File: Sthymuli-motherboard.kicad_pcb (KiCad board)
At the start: 2 copper layers, 277 parts, among them J1 USB_C_Receptacle_USB2.0_16P, J2 Conn_01x09, J3 Conn_01x03, Q1 Q_NMOS_Depletion_GSD, Q10 NX7002AK, Q11 NX7002AK, Q12 NX7002AK, Q13 NX7002AK, Q14 NX7002AK, Q15 NX7002AK, Q2 Q_NMOS_Depletion_GSD, Q3 Q_NMOS_Depletion_GSD, Q4 Q_NMOS_Depletion_GSD, Q5 Q_NMOS_Depletion_GSD, Q6 Q_NMOS_Depletion_GSD, Q7 PMOS, Q8 NX7002AK, Q9 NX7002AK, SW1 SW_Push, SW10 SW_Push, SW2 SW_Push, SW3 SW_Push, SW4 SW_Push, SW5 SW_Push, SW6 SW_Push, SW7 SW_Push, SW8 SW_Push, SW9 SW_Push, U1 ESP32-S3-WROOM-1, U10 74HC4051, U11 MCP6L01x-xOT, U12 74HC4051, U13 LSM6DS3, U14 LSM6DS3, U15 ITR9909, U16 ITR9909, U17 ITR9909, U18 ITR9909, U19 ITR9909, U2 AP2112K-3.3, U20 ITR9909, U21 ITR9909, U22 ITR9909, U3 BQ76905RGRR, U4 AP62300WU, U5 BQ25713, U6 AP62300WU, U7 MCP23017_SO, U8 AP22913CN4, U9 IRM-H6xxT

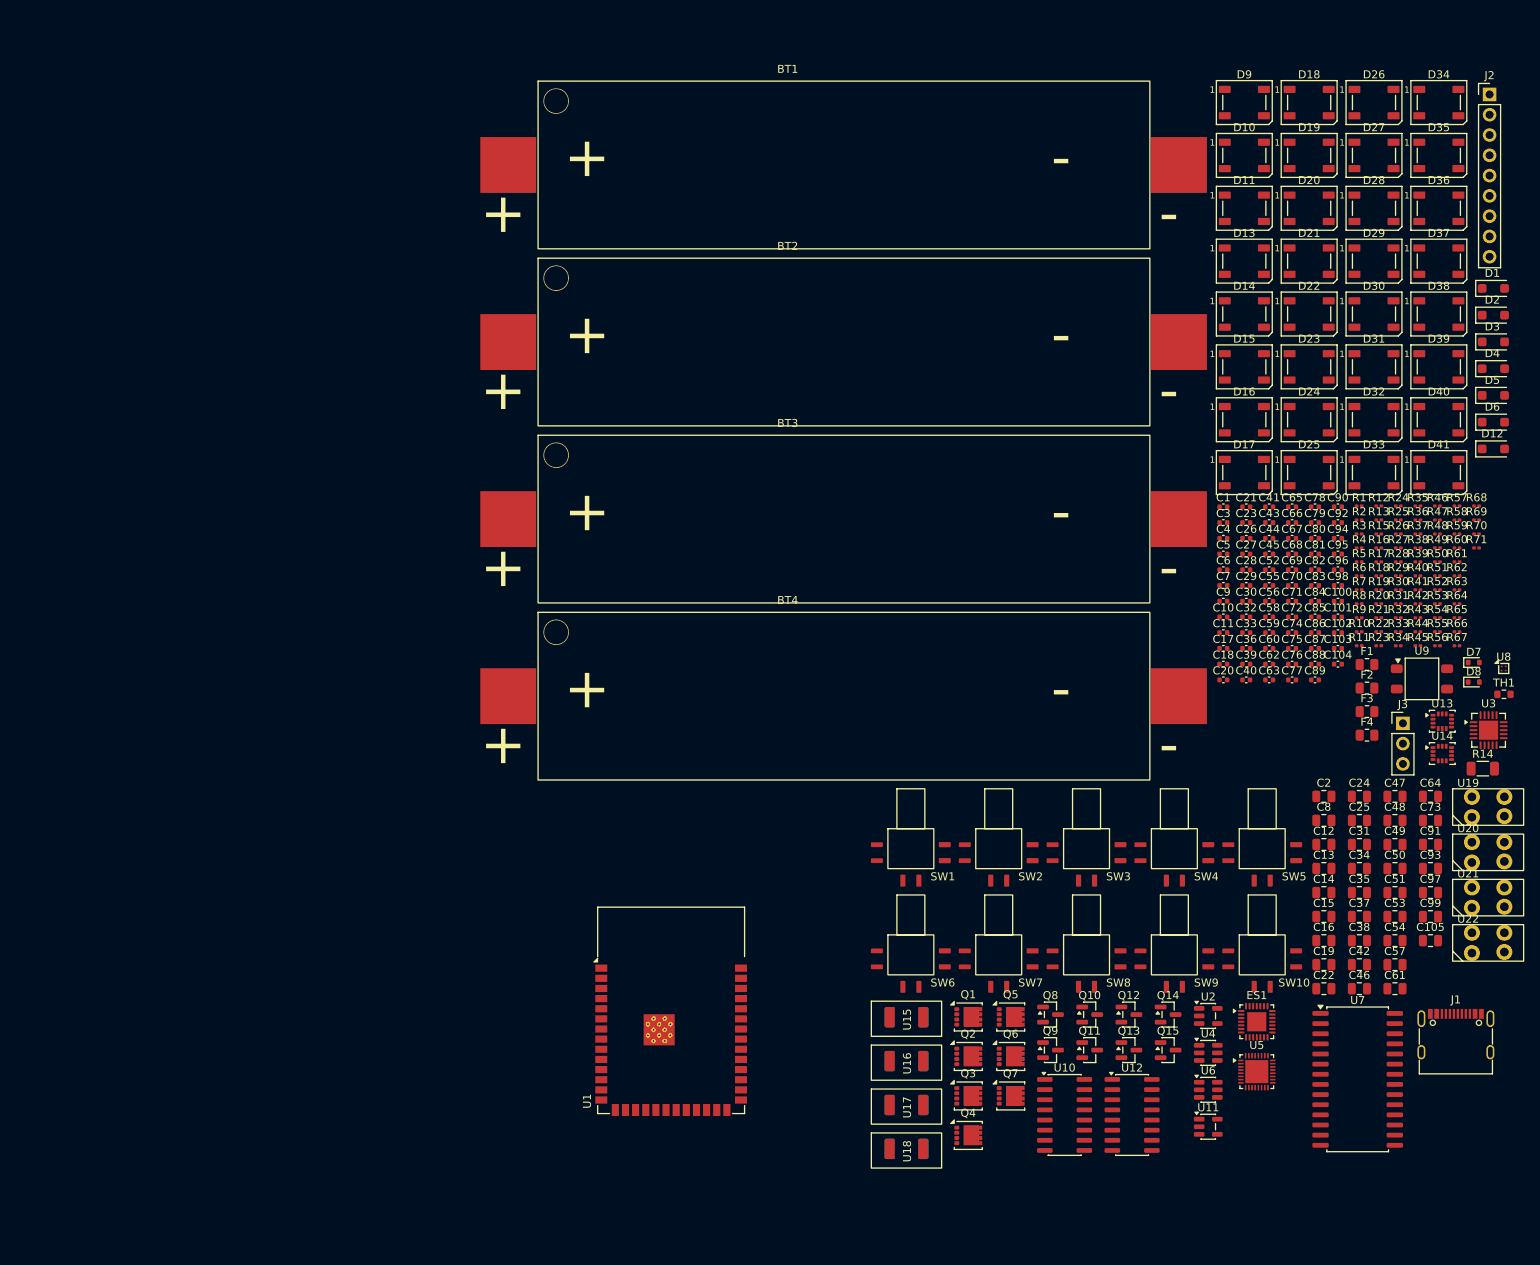
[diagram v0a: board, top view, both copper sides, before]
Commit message: started layout of component
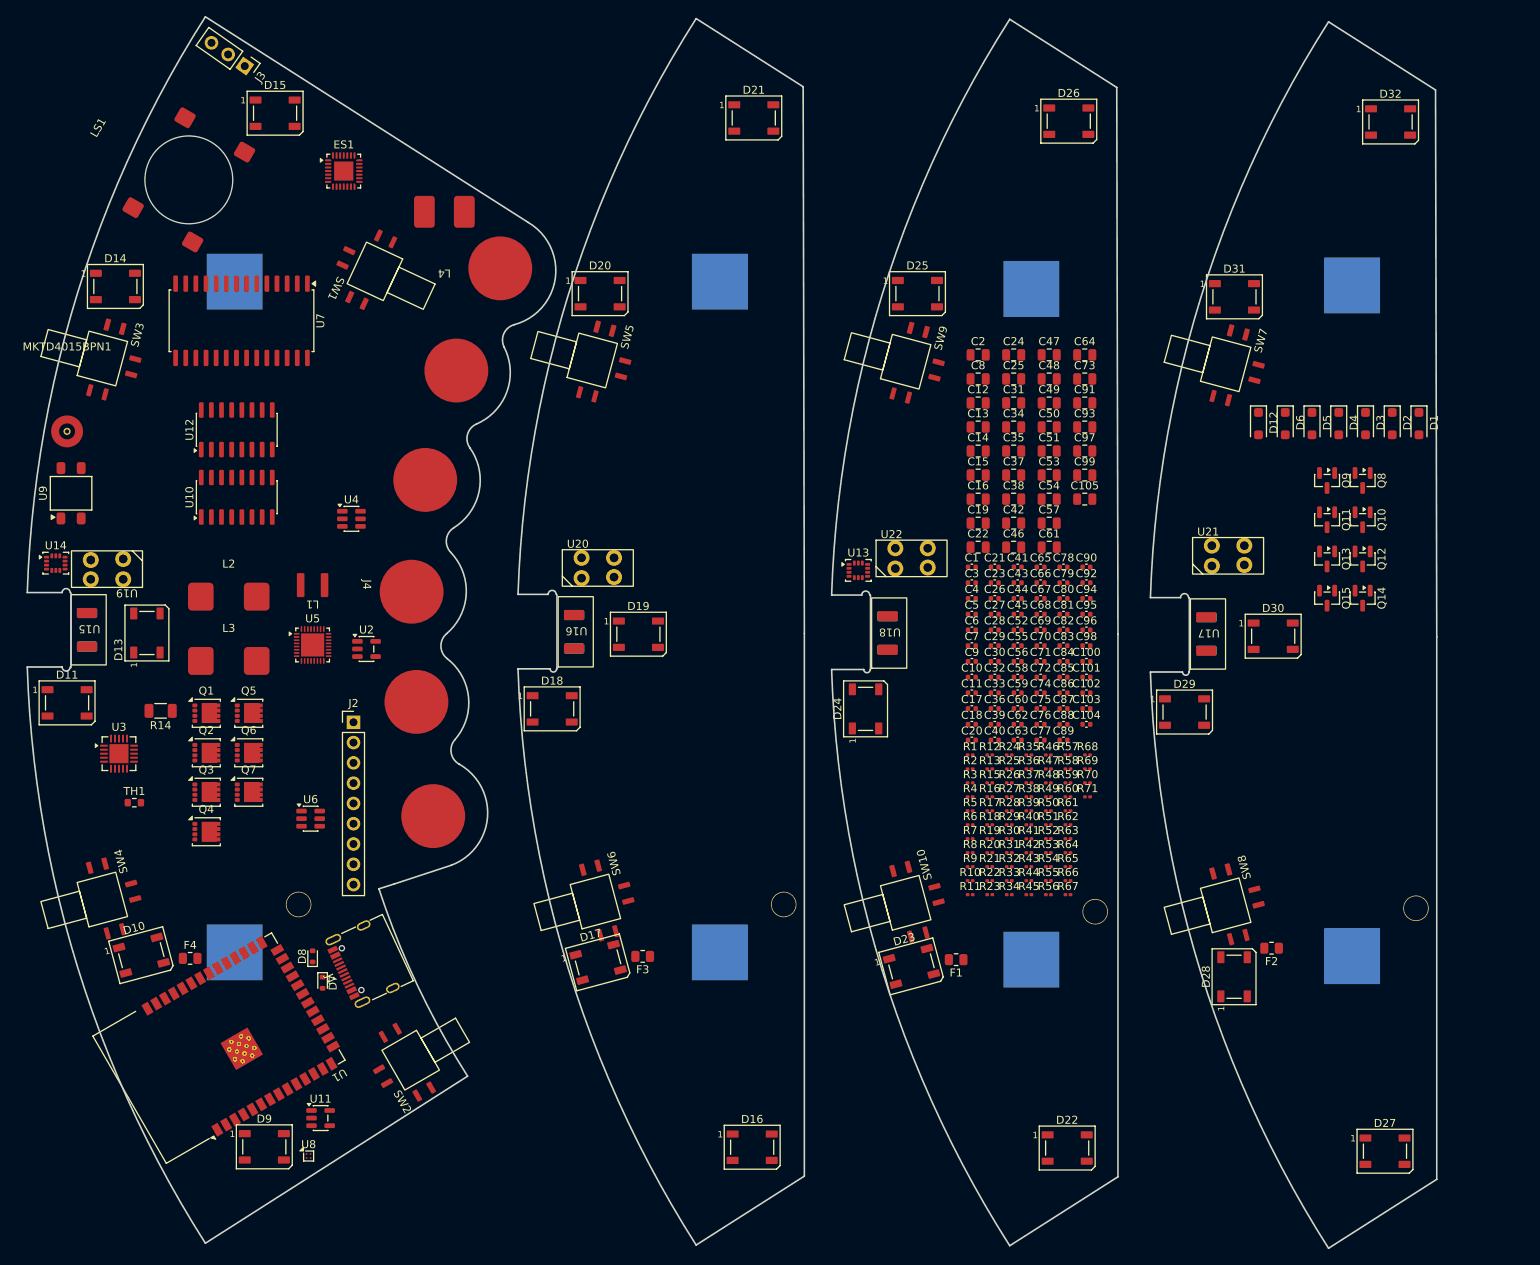
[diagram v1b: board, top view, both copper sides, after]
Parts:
- removed D33, D34, D35, D36, D37, D38, D39, D40, D41: WS2812B, LED_SMD:LED_WS2812B_PLCC4_5.0x5.0mm_P3.2mm
- added J4: Conn_01x06, sthymuli:ConnectorSpring, F.Cu at (34.9, 12.1)
- added L1: 2.2uH, sthymuli:FHD4020S-2R2MT, F.Cu at (48.5, 83.8)
- added L2: 3.3uH, sthymuli:FXL0630-3R3-M, F.Cu at (38.0, 85.2)
- added L3: 3.3uH, sthymuli:FXL0630-3R3-M, F.Cu at (38.0, 93.2)
- added L4: L, sthymuli:TDK VFS5045VA301, F.Cu at (65.0, 37.0)
- added LS1: Speaker, sthymuli:Speaker KELIKING KLJ-01304T-08R07W, F.Cu at (33.0, 33.0)
- added MKTD4015BPN1: Microphone, sthymuli:SAMZO MIC-4013-G-G00, F.Cu at (17.8, 64.5)
- BT1, BT2, BT3, BT4: moved to B.Cu
- moved D9 179.4 mm to (42.5, 154.1)
- moved U19 175.5 mm to (22.8, 81.8), turned to 180 degrees
- moved U14 175.3 mm to (16.3, 81.0)
- moved TH1 172.1 mm to (26.2, 111.0)
- moved U3 171.6 mm to (24.2, 104.9)
- moved U9 170.8 mm to (18.2, 72.2), turned to 90 degrees
- moved D10 170.6 mm to (27.1, 130.1), turned to 15 degrees
- moved U7 169.0 mm to (39.6, 50.6), turned to -90 degrees
- moved J3 166.8 mm to (40.0, 18.8), turned to -125 degrees
- moved R14 165.7 mm to (29.5, 99.5), turned to 180 degrees
- moved J2 162.6 mm to (53.6, 100.9)
- moved U8 161.6 mm to (48.0, 155.2)
- moved D11 159.9 mm to (17.8, 98.5)
- moved ES1 156.3 mm to (52.4, 31.9)
- moved F4 150.0 mm to (33.2, 130.5)
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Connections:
- U5 pad 33: (no net) -> unconnected-(U5-thermal_pad-Pad33)
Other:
- board outline added: 176.5 x 154.2 mm

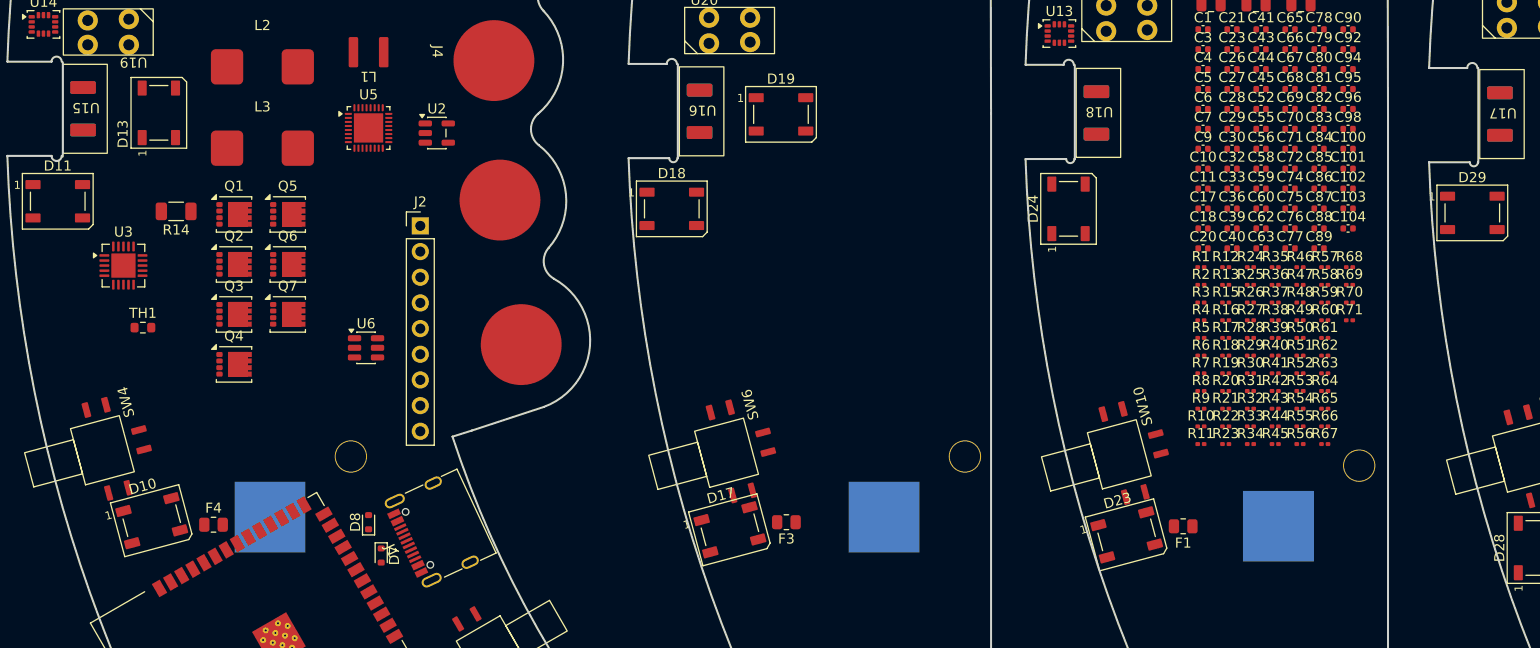
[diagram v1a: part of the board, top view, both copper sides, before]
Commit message: closing edgecut
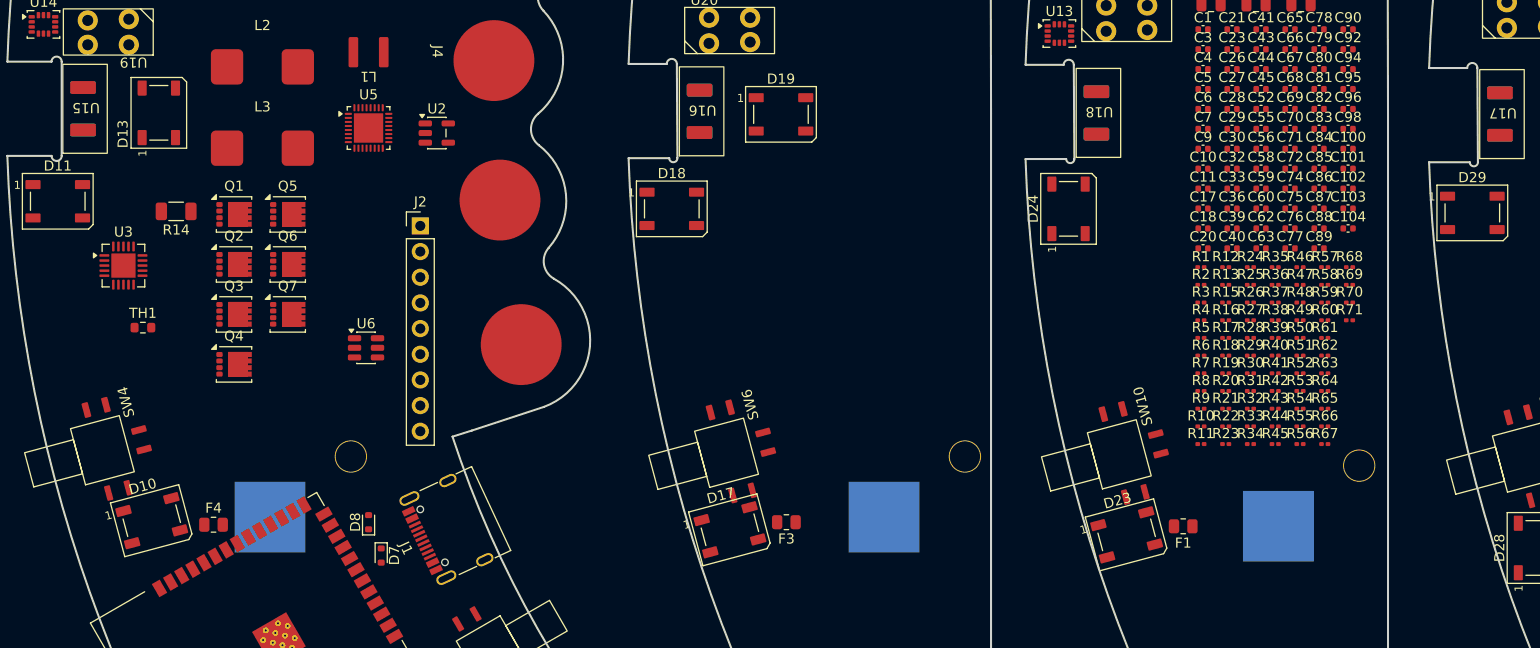
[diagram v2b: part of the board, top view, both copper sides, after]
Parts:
- moved J1 1.47 mm to (57.2, 130.5)
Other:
- outline, holes or cut-outs redrawn
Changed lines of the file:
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@@
 		(fp_poly
 			(pts
-				(xy -1.749999 -8.000001) (xy -1.75 -3.000001) (xy 1.75 -3) (xy 1.75 -8)
+				(xy -1.749999 -8.000002) (xy -1.75 -3.000001) (xy 1.75 -3) (xy 1.75 -8)
 			)
 			(stroke
@@
 	(footprint "Connector_USB:USB_C_Receptacle_G-Switch_GT-USB-7010ASV"
 		(layer "F.Cu")
-		(at 55.75 130.75 115)
+		(at 57.2 130.5 115)
 		(descr "USB Type C, right-angle, SMT, https://datasheet.lcsc.com/lcsc/2204071530_G-Switch-GT-USB-7010ASV_C2988369.pdf")
 		(tags "USB C Type-C Receptacle SMD")
@@
 		)
 		(fp_line
-			(start -4.58 -1.85)
+			(start -4.579999 -1.85)
 			(end -4.58 0.07)
 			(stroke
@@
 		)
 		(fp_text user "${REFERENCE}"
-			(at 0 -9.779 75)
+			(at -0.000001 -9.779 75)
 			(unlocked yes)
 			(layer "F.Fab")
@@
 		(fp_poly
 			(pts
-				(xy -1.750001 -8) (xy -1.75 -3) (xy 1.75 -3) (xy 1.75 -8)
+				(xy -1.750001 -8) (xy -1.75 -3) (xy 1.749999 -3) (xy 1.749999 -8)
 			)
 			(stroke
@@
 		)
 		(pad "39" smd rect
-			(at 8.75 -3.989999 120)
+			(at 8.75 -3.989998 120)
 			(size 1.5 0.9)
 			(layers "F.Cu" "F.Mask" "F.Paste")
@@
 	)
 	(gr_line
-		(start 79.097407 84.929406)
-		(end 79.097407 94.25)
+		(start 78.999743 84.929406)
+		(end 79.055499 94.2)
 		(stroke
 			(width 0.2)
-			(type default)
+			(type solid)
 		)
 		(layer "Edge.Cuts")
@@
 	)
 	(gr_line
-		(start 118.370375 85.01598)
-		(end 118.370375 94.336574)
+		(start 118.272968 85.000004)
+		(end 118.328467 94.304622)
 		(stroke
 			(width 0.2)
@@
 		(stroke
 			(width 0.2)
-			(type default)
+			(type solid)
 		)
 		(layer "Edge.Cuts")
@@
 	)
 	(gr_line
-		(start 18.25 84.75)
-		(end 18.25 94.070483)
+		(start 18.13627 84.686798)
+		(end 18.136254 94.0073)
 		(stroke
 			(width 0.2)
@@
 	)
 	(gr_line
-		(start 158.295647 85.33378)
-		(end 158.295647 94.654374)
+		(start 158.197904 85.33378)
+		(end 158.253739 94.622445)
 		(stroke
 			(width 0.2)

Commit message: fixed some footprint issue, advanced layout
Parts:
- removed C100, C101, C102, C103, C104: 100nF, Capacitor_SMD:C_0402_1005Metric
- removed C105: 10uF, Capacitor_SMD:C_0805_2012Metric
- removed C99: 1uF, Capacitor_SMD:C_0805_2012Metric
- removed the D1 at (187.1, 63.5)
- removed the D12 at (167.0, 63.5)
- removed the D2 at (183.7, 63.5)
- removed the D3 at (180.4, 63.5)
- removed the D4 at (177.0, 63.5)
- removed the D6 at (170.3, 63.5)
- added D17: WS2812B, LED_SMD:LED_WS2812B_PLCC4_5.0x5.0mm_P3.2mm, F.Cu at (126.9, 89.7)
- added D26: D_Schottky, Diode_SMD:D_SOD-123F, F.Cu at (129.4, 134.3)
- added D27: D_Schottky, Diode_SMD:D_SOD-123F, F.Cu at (169.3, 133.5)
- added D28: D_Schottky, Diode_SMD:D_SOD-123F, F.Cu at (90.8, 135.0)
- added D29: D_Schottky, Diode_SMD:D_SOD-123F, F.Cu at (32.2, 125.6)
- added D30: D, Diode_SMD:D_SOD-123F, F.Cu at (54.4, 103.3)
- added D31: D, Diode_SMD:D_SOD-123F, F.Cu at (54.3, 107.1)
- added D34: D, Diode_SMD:D_SOD-123F, F.Cu at (48.2, 126.7)
- C11, C9: value 100pF -> 100nF
- C12, C13, C8: value 1uF -> 100nF; footprint Capacitor_SMD:C_0805_2012Metric -> Capacitor_SMD:C_0402_1005Metric
- C14, C15, C16, C19: value 10uF -> 100nF; footprint Capacitor_SMD:C_0805_2012Metric -> Capacitor_SMD:C_0402_1005Metric
- C17: value 1.8nF -> 100nF
- C18: value 470nF -> 100nF
- C2: value 22 uF -> 100nF; footprint Capacitor_SMD:C_0805_2012Metric -> Capacitor_SMD:C_0402_1005Metric
- C20: value 33pF -> 100nF
- C21: value 15pF -> 100nF
- C22: value 680pF -> 100nF; footprint Capacitor_SMD:C_0805_2012Metric -> Capacitor_SMD:C_0402_1005Metric
- C24, C25: value 33nF -> 100nF; footprint Capacitor_SMD:C_0805_2012Metric -> Capacitor_SMD:C_0402_1005Metric
- C26: value 10nF -> 220nF
- C27, C28, C29: value 10uF -> 220nF
- C3, C4, C5, C6, C7: value 220nF -> 100nF
- C30: value 47nF -> 1uF; footprint Capacitor_SMD:C_0402_1005Metric -> Capacitor_SMD:C_0805_2012Metric
- C31: value 10uF -> 100pF; footprint Capacitor_SMD:C_0805_2012Metric -> Capacitor_SMD:C_0402_1005Metric
- C33: value 47nF -> 100pF
- C34, C35: value 10uF -> 1uF
- C36, C56, C84, C88, C95: value 100nF -> 10uF; footprint Capacitor_SMD:C_0402_1005Metric -> Capacitor_SMD:C_0805_2012Metric
- C37, C38: value 22uF -> 10uF
- C39: value 100pF -> 1.8nF
- C40: value 100pF -> 470nF
- C41: value 100pF -> 10uF; footprint Capacitor_SMD:C_0402_1005Metric -> Capacitor_SMD:C_0805_2012Metric
- C42: value 2.2uF -> 33pF; footprint Capacitor_SMD:C_0805_2012Metric -> Capacitor_SMD:C_0402_1005Metric
- C43: value 100nF -> 15pF
- C44: value 100pF -> 680pF; footprint Capacitor_SMD:C_0402_1005Metric -> Capacitor_SMD:C_0805_2012Metric
- C46: value 22uF -> 33nF
- C47: value 1uF -> 33nF
- C48: value 1uF -> 10nF; footprint Capacitor_SMD:C_0805_2012Metric -> Capacitor_SMD:C_0402_1005Metric
- C49: value 22uF -> 10uF; footprint Capacitor_SMD:C_0805_2012Metric -> Capacitor_SMD:C_0402_1005Metric
- C50: value 10nF -> 10uF; footprint Capacitor_SMD:C_0805_2012Metric -> Capacitor_SMD:C_0402_1005Metric
- C51: value 1.5nF -> 10uF; footprint Capacitor_SMD:C_0805_2012Metric -> Capacitor_SMD:C_0402_1005Metric
- C52: value 330pF -> 47nF
- C53: value 4.7uF -> 10uF
- C54: value 10nF -> 100nF; footprint Capacitor_SMD:C_0805_2012Metric -> Capacitor_SMD:C_0402_1005Metric
- C55: value 100nF -> 47nF
- C57: value 1uF -> 10uF
- C58: value 1nF -> 100nF
- C59: value 1uF -> 22uF; footprint Capacitor_SMD:C_0402_1005Metric -> Capacitor_SMD:C_0805_2012Metric
- C60: value 1nF -> 22uF; footprint Capacitor_SMD:C_0402_1005Metric -> Capacitor_SMD:C_0805_2012Metric
- C61: value 1uF -> 100pF; footprint Capacitor_SMD:C_0805_2012Metric -> Capacitor_SMD:C_0402_1005Metric
- C62, C63: value 100nF -> 100pF
- C64: value 10uF -> 2.2uF
- C66: value 20pF -> 100pF
- C68, C71: value 100nF -> 22uF; footprint Capacitor_SMD:C_0402_1005Metric -> Capacitor_SMD:C_0805_2012Metric
- C69: value 20pF -> 1uF; footprint Capacitor_SMD:C_0402_1005Metric -> Capacitor_SMD:C_0805_2012Metric
- C70, C79, C83, C90, C92: value 100nF -> 1uF; footprint Capacitor_SMD:C_0402_1005Metric -> Capacitor_SMD:C_0805_2012Metric
- C72, C76: value 100nF -> 10nF; footprint Capacitor_SMD:C_0402_1005Metric -> Capacitor_SMD:C_0805_2012Metric
- C73: value 10uF -> 1.5nF
- C74: value 100nF -> 330pF
- C75: value 100nF -> 4.7uF; footprint Capacitor_SMD:C_0402_1005Metric -> Capacitor_SMD:C_0805_2012Metric
- C80, C82: value 100nF -> 1nF
- C81: value 100nF -> 1uF
- C85, C87: value 100nF -> 20pF
- C97: value 1uF -> 22 uF
- C98: value 100nF -> 220nF
- D5: value D -> WS2812B; footprint Diode_SMD:D_SOD-123F -> LED_SMD:LED_WS2812B_PLCC4_5.0x5.0mm_P3.2mm
- moved C64 268.4 mm to (-75.5, 207.7)
- moved C73 257.9 mm to (-71.0, 198.6)
- moved C47 254.7 mm to (-75.5, 189.6)
- moved C46 254.7 mm to (-79.9, 213.7)
- moved C97 254.2 mm to (-66.5, 207.7)
- moved C37 253.1 mm to (-79.9, 201.6)
- moved C38 253.1 mm to (-79.9, 204.6)
- moved C93 252.6 mm to (-66.5, 201.6)
- moved C35 251.6 mm to (-79.9, 195.6)
- moved C34 251.6 mm to (-79.9, 192.6)
- moved C91 250.9 mm to (-66.5, 195.6)
- moved C41 250.7 mm to (-79.9, 207.7)
- moved C44 250.3 mm to (-79.9, 210.7)
- moved C53 248.6 mm to (-75.5, 192.6)
- moved C57 248.6 mm to (-75.5, 198.6)
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- renumbered D13 to D1, D18 to D10, D19 to D11, D20 to D12, D21 to D13, D22 to D14, D23 to D15, D24 to D16, D25 to D18, D26 to D19, D9 to D2, D27 to D20, D28 to D21, D29 to D22, D30 to D23, D31 to D24, D32 to D25, D10 to D3, D7 to D32, D8 to D33, D11 to D4, D14 to D6, D15 to D7, D16 to D8, D17 to D9
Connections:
- BT1 pad 1: +BATT -> Net-(BT1-+)
- BT2 pad 1: Net-(BT1--) -> Net-(BT2-+)
- BT3 pad 1: Net-(BT2--) -> Net-(BT3-+)
- BT4 pad 1: Net-(BT3--) -> Net-(BT4-+)
- C1 pad 1: Net-(U1-3V3) -> Net-(D1-VDD)
- C10 pad 1: Net-(U3-SRP) -> +5V
- C10 pad 2: Net-(U3-SRN) -> GND
- C11 pad 1: Net-(U3-BAT) -> +5V
- C12 pad 1: Net-(U5-VDDA) -> +5V
- C13 pad 1: Net-(U3-BAT) -> +5V
- C14 pad 1: Net-(C14-Pad1) -> +5V
- C15 pad 1: Net-(C14-Pad1) -> +5V
- C16 pad 1: Net-(C14-Pad1) -> +5V
- C17 pad 1: Net-(C17-Pad1) -> +5V
- C18 pad 1: Net-(U5-VBUS) -> +5V
- C19 pad 1: Net-(C14-Pad1) -> +5V
- C2 pad 1: Net-(U1-3V3) -> +5V
- C20 pad 1: Net-(U5-COMP1) -> +5V
- C21 pad 1: Net-(U5-COMP2) -> +5V
- C22 pad 1: Net-(C22-Pad1) -> +5V
- C23 pad 1: RST -> +5V
- C24 pad 1: Net-(U5-ACP) -> +5V
- C25 pad 1: Net-(U5-ACN) -> +5V
- C26 pad 1: Net-(Q3-D) -> GND
- C26 pad 2: GND -> Net-(U3-VC1)
- C27 pad 1: Net-(Q6-D) -> Net-(U3-VC4A)
- C27 pad 2: GND -> Net-(U3-VC5)
- C28 pad 1: Net-(Q6-D) -> Net-(U3-VC2)
- C28 pad 2: GND -> Net-(U3-VC4A)
- C29 pad 1: Net-(Q6-D) -> GND
- C29 pad 2: GND -> Net-(U3-VC0)
- C3 pad 1: Net-(U3-VC1) -> +5V
- C3 pad 2: Net-(U3-VC2) -> GND
- C30 pad 1: Net-(Q3-S) -> Net-(U3-REGSRC)
- C30 pad 2: Net-(U5-BTST1) -> GND
- C31 pad 1: Net-(Q6-D) -> Net-(U3-SRP)
- C31 pad 2: GND -> Net-(U3-SRN)
- C32 pad 1: BOOT_MODE -> Net-(U3-SRP)
- C32 pad 2: GND -> Net-(U3-SRN)
- C33 pad 1: Net-(Q5-D) -> Net-(U3-BAT)
- C33 pad 2: Net-(U5-BTST2) -> GND
- C34 pad 1: Net-(Q6-D) -> Net-(U5-VDDA)
- C35 pad 1: Net-(Q6-D) -> Net-(U3-BAT)
- C36 pad 1: Net-(U4-BST) -> Net-(C36-Pad1)
- C36 pad 2: Net-(U4-SW) -> GND
- C37 pad 1: GND -> Net-(C36-Pad1)
- C37 pad 2: Net-(U1-3V3) -> GND
- C38 pad 1: GND -> Net-(C36-Pad1)
- C38 pad 2: Net-(U1-3V3) -> GND
- C39 pad 1: Net-(U4-FB) -> Net-(C39-Pad1)
- C39 pad 2: Net-(U1-3V3) -> GND
- C4 pad 1: GND -> +5V
- C4 pad 2: Net-(U3-VC1) -> GND
- C40 pad 1: Net-(U5-IBAT) -> Net-(U5-VBUS)
- C41 pad 1: Net-(U5-IADPT) -> Net-(C36-Pad1)
- C42 pad 1: GND -> Net-(U5-COMP1)
- C42 pad 2: Net-(U5-REGN) -> GND
- C43 pad 1: Net-(U6-BST) -> Net-(U5-COMP2)
- C43 pad 2: Net-(U6-SW) -> GND
- C44 pad 1: Net-(U6-FB) -> Net-(C44-Pad1)
- C44 pad 2: +5V -> GND
- C45 pad 1: +BATT -> RST
- C45 pad 2: Net-(Q7-D) -> GND
- C46 pad 1: GND -> Net-(U5-ACP)
- C46 pad 2: +5V -> GND
- C47 pad 1: GND -> Net-(U5-ACN)
- C47 pad 2: +3V3 -> GND
- C48 pad 1: GND -> Net-(Q3-D)
- C48 pad 2: Net-(Q7-D) -> GND
- C49 pad 1: GND -> Net-(Q6-D)
- C49 pad 2: +5V -> GND
- C5 pad 1: Net-(U3-VC4A) -> +5V
- C5 pad 2: Net-(U3-VC5) -> GND
- C50 pad 1: GND -> Net-(Q6-D)
- C50 pad 2: +3V3 -> GND
- C51 pad 1: Net-(U11--) -> Net-(Q6-D)
- C51 pad 2: Net-(C51-Pad2) -> GND
- C52 pad 1: IR_analog -> Net-(Q3-S)
- C52 pad 2: Net-(U11--) -> Net-(U5-BTST1)
- C53 pad 1: Net-(U9-Vcc) -> Net-(Q6-D)
- C54 pad 1: GND -> BOOT_MODE
- C54 pad 2: +3V3 -> GND
- C55 pad 1: +3V3 -> Net-(Q5-D)
- C55 pad 2: GND -> Net-(U5-BTST2)
- C56 pad 1: +3V3 -> Net-(Q6-D)
- C57 pad 1: /MIC_P -> Net-(Q6-D)
- C57 pad 2: Net-(MKTD4015BPN1-+) -> GND
- C58 pad 1: Net-(MKTD4015BPN1-+) -> Net-(U4-BST)
- C58 pad 2: GND -> Net-(U4-SW)
- C59 pad 1: /MIC_N -> GND
- C59 pad 2: Net-(MKTD4015BPN1--) -> Net-(U1-3V3)
- C6 pad 1: Net-(U3-VC2) -> +5V
- C6 pad 2: Net-(U3-VC4A) -> GND
- C60 pad 1: Net-(MKTD4015BPN1--) -> GND
- C60 pad 2: GND -> Net-(U1-3V3)
- C61 pad 1: Net-(C61-Pad1) -> Net-(U4-FB)
- C61 pad 2: GND -> Net-(U1-3V3)
- C62 pad 1: +5V -> Net-(U5-IBAT)
- C63 pad 1: +5V -> Net-(U5-IADPT)
- C64 pad 1: +3V3 -> GND
- C64 pad 2: GNDA -> Net-(U5-REGN)
- C65 pad 1: Net-(D12-K) -> Net-(U6-BST)
- C65 pad 2: GND -> Net-(U6-SW)
- C66 pad 1: Net-(ES1-CCLK) -> Net-(U6-FB)
- C66 pad 2: GND -> +5V
- C67 pad 1: +3V3 -> +BATT
- C67 pad 2: GNDA -> Net-(Q7-D)
- C68 pad 1: +5V -> GND
- C68 pad 2: GND -> +5V
- C69 pad 1: Net-(ES1-CDATA) -> GND
- C69 pad 2: GND -> +3V3
- C7 pad 1: GND -> +5V
- C7 pad 2: Net-(U3-VC0) -> GND
- C70 pad 1: +5V -> GND
- C70 pad 2: GND -> Net-(Q7-D)
- C71 pad 1: +5V -> GND
- C71 pad 2: GND -> +5V
- C72 pad 1: +5V -> GND
- C72 pad 2: GND -> +3V3
- C73 pad 1: Net-(ES1-SPKVDD) -> Net-(U11--)
- C73 pad 2: GNDA -> Net-(C73-Pad2)
- C74 pad 1: +5V -> IR_analog
- C74 pad 2: GND -> Net-(U11--)
- C75 pad 1: Net-(ES1-SPKVDD) -> Net-(U9-Vcc)
- C75 pad 2: GNDA -> GND
- C76 pad 1: +5V -> GND
- C76 pad 2: GND -> +3V3
- C77 pad 1: +5V -> +3V3
- C78 pad 1: +5V -> +3V3
- C79 pad 1: +5V -> /MIC_P
- C79 pad 2: GND -> Net-(MKTD4015BPN1-+)
- C8 pad 1: Net-(U3-REGSRC) -> +5V
- C80 pad 1: +5V -> Net-(MKTD4015BPN1-+)
- C81 pad 1: +5V -> /MIC_N
- C81 pad 2: GND -> Net-(MKTD4015BPN1--)
- C82 pad 1: +5V -> Net-(MKTD4015BPN1--)
- C83 pad 1: +5V -> Net-(C83-Pad1)
- C84 pad 1: +5V -> +3V3
- C84 pad 2: GND -> GNDA
- C85 pad 1: +5V -> Net-(ES1-CCLK)
- C86 pad 1: +5V -> +3V3
- C86 pad 2: GND -> GNDA
- C87 pad 1: +5V -> Net-(ES1-CDATA)
- C88 pad 1: +5V -> Net-(ES1-SPKVDD)
- C88 pad 2: GND -> GNDA
- C89 pad 1: +5V -> Net-(ES1-SPKVDD)
- C89 pad 2: GND -> GNDA
- C9 pad 1: Net-(U3-SRP) -> +5V
- C9 pad 2: Net-(U3-SRN) -> GND
- C90 pad 1: +5V -> Net-(ES1-DAC/REF)
- C90 pad 2: GND -> GNDA
- C91 pad 1: Net-(ES1-DAC/REF) -> Net-(ES1-ADC/REF)
- C92 pad 1: +5V -> Net-(ES1-VMID)
- C92 pad 2: GND -> GNDA
- C93 pad 1: Net-(ES1-ADC/REF) -> /MICBIAS
- C94 pad 1: +5V -> GNDA
- C94 pad 2: GND -> +3V3
- C95 pad 1: +5V -> GNDA
- C95 pad 2: GND -> +3V3
- C96 pad 1: +5V -> Net-(U1-3V3)
- C97 pad 1: Net-(ES1-VMID) -> Net-(U1-3V3)
- C97 pad 2: GNDA -> GND
- C98 pad 1: +5V -> Net-(U3-VC1)
- C98 pad 2: GND -> Net-(U3-VC2)
- D1 pad 1: Net-(D12-K) -> Net-(D1-VDD)
- D1 pad 2: Net-(D13-DOUT) -> Net-(D1-DOUT)
- D10 pad 2: Net-(D18-DOUT) -> Net-(D10-DOUT)
- D10 pad 4: Net-(D14-DOUT) -> Net-(D10-DIN)
- D11 pad 2: Net-(D19-DOUT) -> Net-(D11-DOUT)
- D11 pad 4: Net-(D15-DOUT) -> Net-(D10-DOUT)
- D12 pad 2: Net-(D20-DOUT) -> Net-(D12-DOUT)
- D12 pad 4: Net-(D16-DOUT) -> Net-(D11-DOUT)
- D13 pad 2: Net-(D21-DOUT) -> Net-(D13-DOUT)
- D13 pad 4: Net-(D17-DOUT) -> Net-(D12-DOUT)
- D14 pad 2: Net-(D22-DOUT) -> Net-(D14-DOUT)
- D14 pad 4: Net-(D18-DOUT) -> Net-(D13-DOUT)
- D15 pad 2: Net-(D23-DOUT) -> Net-(D15-DOUT)
- D15 pad 4: Net-(D19-DOUT) -> Net-(D14-DOUT)
- D16 pad 2: Net-(D24-DOUT) -> Net-(D16-DOUT)
- D16 pad 4: Net-(D20-DOUT) -> Net-(D15-DOUT)
- D18 pad 2: Net-(D25-DOUT) -> Net-(D18-DOUT)
- D18 pad 4: Net-(D21-DOUT) -> Net-(D17-DOUT)
- D19 pad 2: Net-(D26-DOUT) -> Net-(D19-DOUT)
- D19 pad 4: Net-(D22-DOUT) -> Net-(D18-DOUT)
- D2 pad 2: Net-(D14-DIN) -> Net-(D2-DOUT)
- D2 pad 4: Net-(D41-DOUT) -> Net-(D1-DOUT)
- D20 pad 2: Net-(D27-DOUT) -> Net-(D20-DOUT)
- D20 pad 4: Net-(D23-DOUT) -> Net-(D19-DOUT)
- D21 pad 2: Net-(D28-DOUT) -> Net-(D21-DOUT)
- D21 pad 4: Net-(D24-DOUT) -> Net-(D20-DOUT)
- D22 pad 2: Net-(D29-DOUT) -> Net-(D22-DOUT)
- D22 pad 4: Net-(D25-DOUT) -> Net-(D21-DOUT)
- D23 pad 2: Net-(D30-DOUT) -> Net-(D23-DOUT)
- D23 pad 4: Net-(D26-DOUT) -> Net-(D22-DOUT)
- D24 pad 2: Net-(D31-DOUT) -> Net-(D24-DOUT)
- D24 pad 4: Net-(D27-DOUT) -> Net-(D23-DOUT)
- D25 pad 2: Net-(D32-DOUT) -> unconnected-(D25-DOUT-Pad2)
- D25 pad 4: Net-(D28-DOUT) -> Net-(D24-DOUT)
- D3 pad 2: Net-(D10-DOUT) -> Net-(D3-DOUT)
- D3 pad 4: Net-(D10-DIN) -> Net-(D2-DOUT)
- D4 pad 2: Net-(D11-DOUT) -> Net-(D4-DOUT)
- D4 pad 4: Net-(D11-DIN) -> Net-(D3-DOUT)
- D5 pad 1: Net-(D5-K) -> +5V
- D5 pad 2: +BATT -> Net-(D5-DOUT)
- D6 pad 2: Net-(D14-DOUT) -> Net-(D6-DOUT)
- D6 pad 4: Net-(D14-DIN) -> Net-(D5-DOUT)
- D7 pad 2: Net-(D15-DOUT) -> Net-(D7-DOUT)
- D7 pad 4: Net-(D10-DOUT) -> Net-(D6-DOUT)
- D8 pad 2: Net-(D16-DOUT) -> Net-(D8-DOUT)
- D8 pad 4: Net-(D11-DOUT) -> Net-(D7-DOUT)
- D9 pad 2: Net-(D17-DOUT) -> Net-(D10-DIN)
- D9 pad 4: Net-(D13-DOUT) -> Net-(D8-DOUT)
- F1 pad 2: Net-(D1-K) -> Net-(BT1-+)
- F2 pad 2: Net-(D2-K) -> Net-(BT2-+)
- F3 pad 2: Net-(D3-K) -> Net-(BT3-+)
- F4 pad 2: Net-(D4-K) -> Net-(BT4-+)
- R11 pad 1: Net-(C14-Pad1) -> Net-(C36-Pad1)
- R25 pad 2: Net-(C17-Pad1) -> Net-(C39-Pad1)
- R27 pad 2: Net-(C14-Pad1) -> Net-(C36-Pad1)
- R29 pad 2: Net-(C14-Pad1) -> Net-(C36-Pad1)
- R30 pad 2: Net-(C14-Pad1) -> Net-(C36-Pad1)
- R32 pad 2: Net-(C22-Pad1) -> Net-(C44-Pad1)
- R44 pad 1: Net-(C51-Pad2) -> Net-(C73-Pad2)
- R58 pad 1: Net-(C61-Pad1) -> Net-(C83-Pad1)
- R59 pad 1: Net-(C61-Pad1) -> Net-(C83-Pad1)
- R8 pad 1: Net-(D5-K) -> Net-(D30-K)
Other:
- outline, holes or cut-outs redrawn
